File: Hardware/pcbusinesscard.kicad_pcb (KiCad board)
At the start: 2 copper layers, 89 x 51 mm, 0 parts

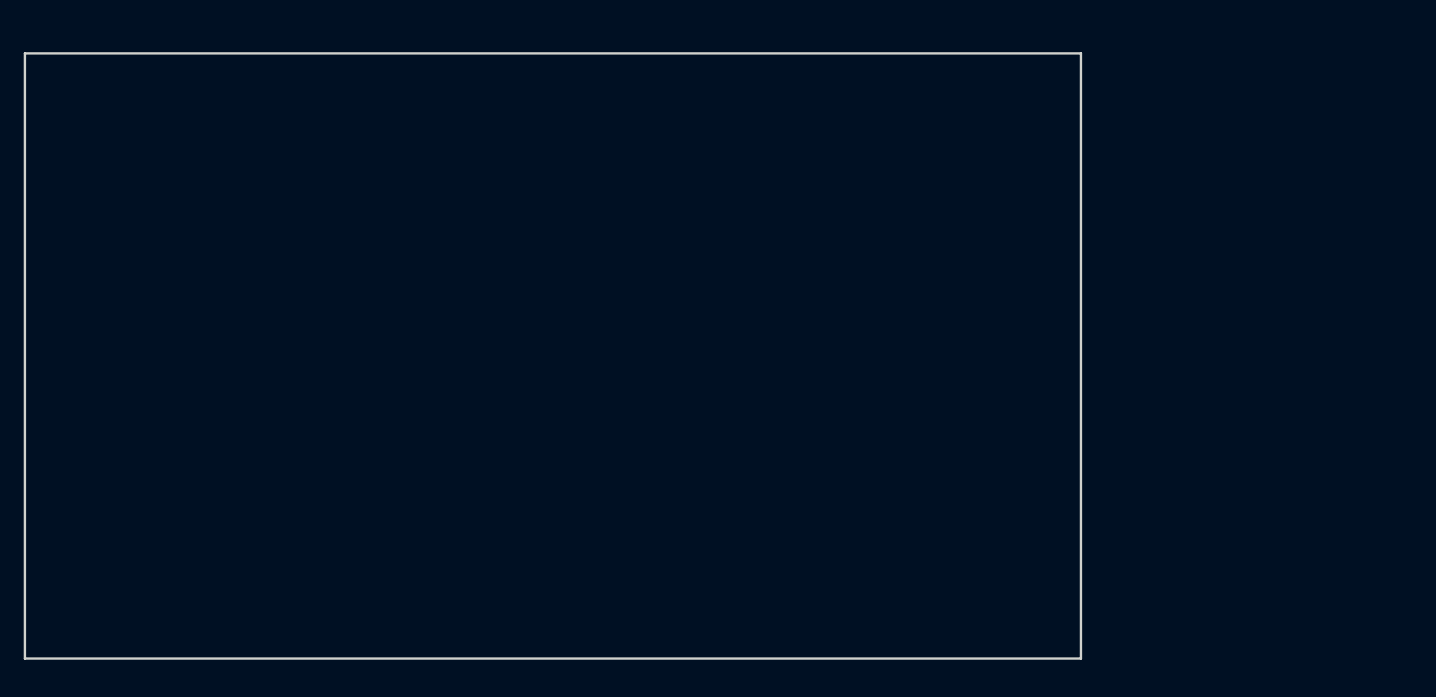
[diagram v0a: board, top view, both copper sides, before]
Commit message: Overhaul entire design with RP2040
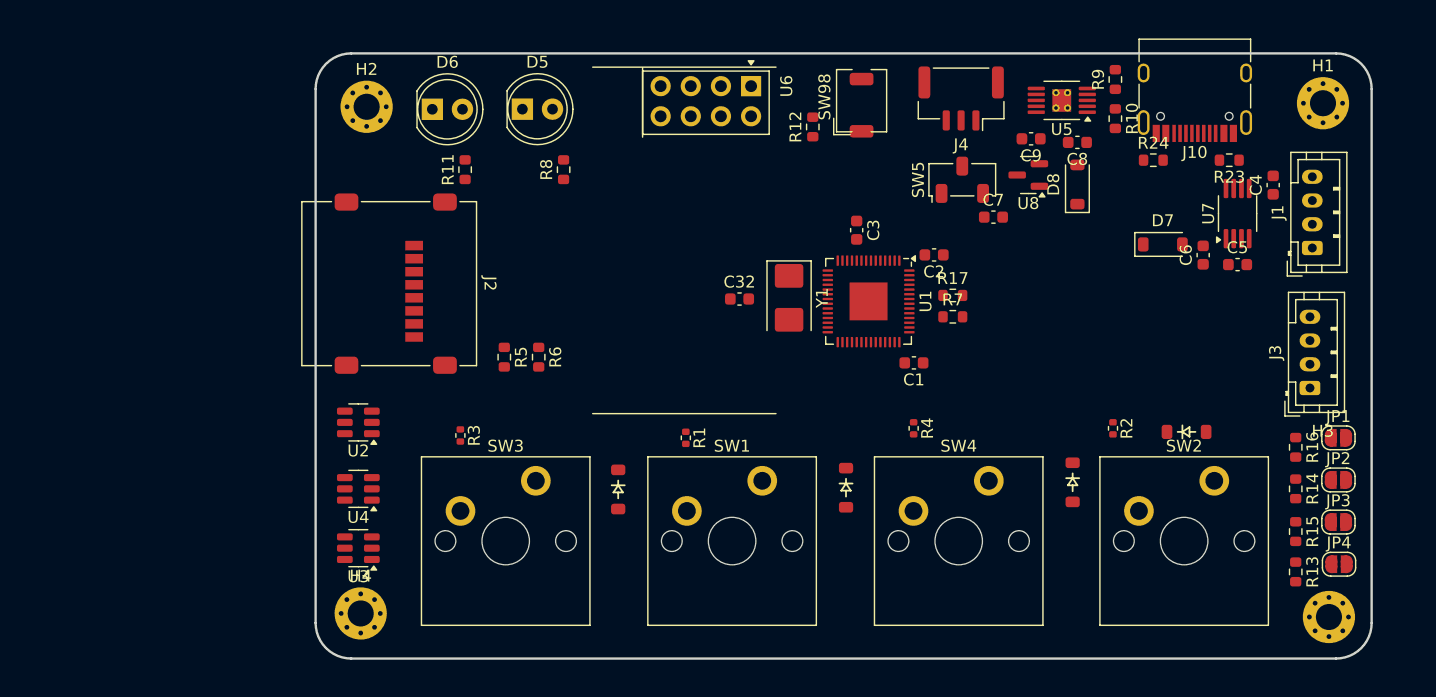
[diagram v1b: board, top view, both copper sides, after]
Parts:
- added C1: 1u, Capacitor_SMD:C_0603_1608Metric, F.Cu at (113.9, 63.1)
- added C2: 1u, Capacitor_SMD:C_0603_1608Metric, F.Cu at (115.6, 54.0)
- added C3: 1u, Capacitor_SMD:C_0603_1608Metric, F.Cu at (109.1, 51.9)
- added C32: 1u, Capacitor_SMD:C_0603_1608Metric, F.Cu at (99.2, 57.7)
- added C4: 1u, Capacitor_SMD:C_0603_1608Metric, F.Cu at (144.2, 48.1)
- added C5: 10n, Capacitor_SMD:C_0603_1608Metric, F.Cu at (141.2, 54.8)
- added C6: 10u, Capacitor_SMD:C_0603_1608Metric, F.Cu at (138.3, 54.0)
- added C7: 1u, Capacitor_SMD:C_0603_1608Metric, F.Cu at (120.6, 50.8)
- added C8: 1u, Capacitor_SMD:C_0603_1608Metric, F.Cu at (127.7, 44.5)
- added C9: 1u, Capacitor_SMD:C_0603_1608Metric, F.Cu at (123.8, 44.2)
- added D1: ESC, ScottoKeebs_Components:Diode_SOD-123, F.Cu at (108.2, 73.6)
- added D2: ~/`, ScottoKeebs_Components:Diode_SOD-123, F.Cu at (136.9, 68.9)
- added D3: 1, ScottoKeebs_Components:Diode_SOD-123, F.Cu at (89.0, 73.8)
- added D4: 2, ScottoKeebs_Components:Diode_SOD-123, F.Cu at (127.3, 73.2)
- added D5: LED_Small, LED_THT:LED_D5.0mm, F.Cu at (80.9, 41.7)
- added D6: LED_Small, LED_THT:LED_D5.0mm, F.Cu at (73.3, 41.7)
- added D7: MBR0520, Diode_SMD:D_SOD-123, F.Cu at (134.9, 53.1)
- added D8: MBR0520, Diode_SMD:D_SOD-123, F.Cu at (127.7, 48.0)
- added H1: MountingHole_Pad, MountingHole:MountingHole_2.2mm_M2_Pad_Via, F.Cu at (148.4, 41.2)
- added H2: MountingHole_Pad, MountingHole:MountingHole_2.2mm_M2_Pad_Via, F.Cu at (67.8, 41.5)
- added H3: MountingHole_Pad, MountingHole:MountingHole_2.2mm_M2_Pad_Via, F.Cu at (148.9, 84.5)
- added H4: MountingHole_Pad, MountingHole:MountingHole_2.2mm_M2_Pad_Via, F.Cu at (67.3, 84.2)
- added J1: Conn_01x04_Pin, Connector_JST:JST_PH_B4B-PH-K_1x04_P2.00mm_Vertical, F.Cu at (147.5, 53.4)
- added J10: USB_C_Receptacle_USB2.0, Connector_USB:USB_C_Receptacle_HRO_TYPE-C-31-M-12, F.Cu at (137.6, 39.7)
- added J2: Micro_SD_Card, Connector_Card:microSD_HC_Molex_47219-2001, F.Cu at (69.7, 56.4)
- added J3: Conn_01x04_Pin, Connector_JST:JST_PH_B4B-PH-K_1x04_P2.00mm_Vertical, F.Cu at (147.3, 65.2)
- added J4: Conn_01x03, Connector_JST:JST_GH_SM03B-GHS-TB_1x03-1MP_P1.25mm_Horizontal, F.Cu at (117.9, 40.8)
- added JP1: SolderJumper_2_Open, Jumper:SolderJumper-2_P1.3mm_Open_RoundedPad1.0x1.5mm, F.Cu at (149.7, 69.4)
- added JP2: SolderJumper_2_Open, Jumper:SolderJumper-2_P1.3mm_Open_RoundedPad1.0x1.5mm, F.Cu at (149.7, 73.0)
- added JP3: SolderJumper_2_Open, Jumper:SolderJumper-2_P1.3mm_Open_RoundedPad1.0x1.5mm, F.Cu at (149.7, 76.5)
- added JP4: SolderJumper_2_Open, Jumper:SolderJumper-2_P1.3mm_Open_RoundedPad1.0x1.5mm, F.Cu at (149.8, 80.1)
- added R1: 100, Resistor_SMD:R_0402_1005Metric, F.Cu at (94.7, 69.4)
- added R10: 1k, Resistor_SMD:R_0603_1608Metric, F.Cu at (130.9, 42.5)
- added R11: 1.5k, Resistor_SMD:R_0603_1608Metric, F.Cu at (76.1, 46.8)
- added R12: 10k, Resistor_SMD:R_0603_1608Metric, F.Cu at (105.4, 43.2)
- added R13: 10k, Resistor_SMD:R_0603_1608Metric, F.Cu at (146.1, 80.7)
- added R14: 10k, Resistor_SMD:R_0603_1608Metric, F.Cu at (146.1, 73.7)
- added R15: 10k, Resistor_SMD:R_0603_1608Metric, F.Cu at (146.1, 77.3)
- added R16: 10k, Resistor_SMD:R_0603_1608Metric, F.Cu at (146.1, 70.2)
- added R17: 22, Resistor_SMD:R_0603_1608Metric, F.Cu at (117.2, 57.4)
- added R2: 100, Resistor_SMD:R_0402_1005Metric, F.Cu at (130.7, 68.6)
- added R23: 5.1K, Resistor_SMD:R_0603_1608Metric, F.Cu at (140.5, 46.0)
- added R24: 5.1K, Resistor_SMD:R_0603_1608Metric, F.Cu at (134.1, 46.0)
- added R3: 100, Resistor_SMD:R_0402_1005Metric, F.Cu at (75.7, 69.2)
- added R4: 100, Resistor_SMD:R_0402_1005Metric, F.Cu at (113.9, 68.6)
- added R5: 4.7k, Resistor_SMD:R_0603_1608Metric, F.Cu at (79.4, 62.6)
- added R6: 4.7k, Resistor_SMD:R_0603_1608Metric, F.Cu at (82.3, 62.6)
- added R7: 22, Resistor_SMD:R_0603_1608Metric, F.Cu at (117.2, 59.2)
- added R8: 1.5k, Resistor_SMD:R_0603_1608Metric, F.Cu at (84.4, 46.8)
- added R9: 2k, Resistor_SMD:R_0603_1608Metric, F.Cu at (130.9, 39.2)
- added SW1: ESC, ScottoKeebs_MX:MX_PCB_1.00u, F.Cu at (98.6, 78.1)
- added SW2: `, ScottoKeebs_MX:MX_PCB_1.00u, F.Cu at (136.7, 78.1)
- added SW3: 1, ScottoKeebs_MX:MX_PCB_1.00u, F.Cu at (79.5, 78.1)
- added SW4: 2, ScottoKeebs_MX:MX_PCB_1.00u, F.Cu at (117.7, 78.1)
- added SW5: SW_Nidec_CAS-120A1, Button_Switch_SMD:Nidec_Copal_CAS-120A, F.Cu at (118.0, 47.6)
- added SW98: SW_Push, ScottoKeebs_Miscellaneous:SW_DIP_SPSTx01_Slide_6.7x4.1mm_W6.73mm_P2.54mm_LowProfile_JPin, F.Cu at (109.5, 43.6)
- added U1: RP2040, Package_DFN_QFN:QFN-56-1EP_7x7mm_P0.4mm_EP3.2x3.2mm, F.Cu at (110.1, 57.9)
- added U2: 24AA025E-OT, Package_TO_SOT_SMD:SOT-23-6, F.Cu at (67.1, 68.1)
- added U3: 24AA025E-OT, Package_TO_SOT_SMD:SOT-23-6, F.Cu at (67.1, 78.7)
- added U4: 24AA025E-OT, Package_TO_SOT_SMD:SOT-23-6, F.Cu at (67.1, 73.7)
- added U5: BQ24090DGQ, Package_SO:HVSSOP-10-1EP_3x3mm_P0.5mm_EP1.57x1.88mm_ThermalVias, F.Cu at (126.4, 41.0)
- added U6: NRF24L01_Breakout, RF_Module:nRF24L01_Breakout, F.Cu at (100.2, 39.8)
- added U7: LT1762-3.3, Package_SO:MSOP-8_3x3mm_P0.65mm, F.Cu at (141.2, 50.5)
- added U8: MCP1700x-330xxTT, Package_TO_SOT_SMD:SOT-23, F.Cu at (123.6, 47.2)
- added Y1: 12MHz, Crystal:Crystal_SMD_5032-2Pin_5.0x3.2mm, F.Cu at (103.4, 57.6)
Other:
- outline, holes or cut-outs redrawn

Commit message: adding to layout
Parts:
- added C10: 1u, Capacitor_SMD:C_0603_1608Metric, F.Cu at (108.4, 64.9)
- added D10: LED_Small, LED_SMD:LED_0805_2012Metric, F.Cu at (136.0, 61.5)
- added D9: LED_Small, LED_SMD:LED_0805_2012Metric, F.Cu at (132.7, 61.5)
- added R18: 1.5k, Resistor_SMD:R_0603_1608Metric, F.Cu at (133.0, 58.0)
- added R19: 1.5k, Resistor_SMD:R_0603_1608Metric, F.Cu at (135.5, 58.0)
- C1: value 1u -> 4.7u
- moved D3 7.19 mm to (89.8, 66.6), turned to 180 degrees
- moved C32 5.52 mm to (102.8, 61.9)
- moved R5 5.30 mm to (84.7, 62.6)
- moved R15 4.40 mm to (146.1, 72.9), turned to 180 degrees
- moved C1 3.42 mm to (117.1, 61.8)
- moved R6 2.91 mm to (79.4, 62.8)
- moved R14 2.70 mm to (146.1, 76.4), turned to 180 degrees
- moved D5 2.55 mm to (83.5, 41.8), turned to 180 degrees
- moved D4 1.85 mm to (127.4, 71.3)
- moved Y1 1.40 mm to (102.0, 57.6)
- moved R13 1.20 mm to (146.0, 79.5), turned to 180 degrees
- moved R16 0.90 mm to (146.1, 69.3), turned to 180 degrees
- moved R17 0.80 mm to (117.2, 58.2)
- moved R7 0.80 mm to (117.2, 60.0)
- moved H3 0.64 mm to (148.5, 84.0)
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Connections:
- net Net-(J10-D+-PadA6) renamed /d+
- net Net-(J10-D--PadA7) renamed /d-
- H1 pad 1: VDD -> VBUS
- H2 pad 1: VBUS -> VBAT
- H3 pad 1: VBAT -> +3.3V
- J1 pad 1: unconnected-(J1-Pin_1-Pad1) -> +3.3V
- J3 pad 1: unconnected-(J3-Pin_1-Pad1) -> +3.3V
- JP1 pad 2: VDD -> +3.3V
- JP2 pad 2: VDD -> +3.3V
- JP3 pad 2: VDD -> +3.3V
- JP4 pad 2: VDD -> +3.3V
- R1 pad 1: VDD -> +3.3V
- R11 pad 1: unconnected-(R11-Pad1) -> VBUS
- R12 pad 1: VDD -> +3.3V
- R2 pad 1: VDD -> +3.3V
- R3 pad 1: VDD -> +3.3V
- R4 pad 1: VDD -> +3.3V
- U1 pad 12: unconnected-(U1-GPIO9-Pad12) -> /SPI1_CS
- U1 pad 13: unconnected-(U1-GPIO10-Pad13) -> /SPI1_SCK
- U1 pad 15: unconnected-(U1-GPIO12-Pad15) -> /SPI1_MISO
- U1 pad 29: unconnected-(U1-GPIO18-Pad29) -> /RP_SCK0
- U1 pad 30: unconnected-(U1-GPIO19-Pad30) -> /RP_SDA0
- U1 pad 31: unconnected-(U1-GPIO20-Pad31) -> /SW_3
- U1 pad 34: unconnected-(U1-GPIO22-Pad34) -> /SW_1
- U1 pad 35: unconnected-(U1-GPIO23-Pad35) -> /SW_4
- U1 pad 36: unconnected-(U1-GPIO24-Pad36) -> /SW_2
- U1 pad 37: unconnected-(U1-GPIO25-Pad37) -> /ADD_B3
- U1 pad 38: unconnected-(U1-GPIO26_ADC0-Pad38) -> /ADD_B2
- U1 pad 39: unconnected-(U1-GPIO27_ADC1-Pad39) -> /ADD_B1
- U1 pad 40: unconnected-(U1-GPIO28_ADC2-Pad40) -> /ADD_B0
- U1 pad 52: /SPI1_SCK -> unconnected-(U1-QSPI_SCLK-Pad52)
- U1 pad 55: /SPI1_MISO -> unconnected-(U1-QSPI_SD1-Pad55)
- U1 pad 9: unconnected-(U1-GPIO7-Pad9) -> /SPI1_MOSI
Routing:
- net +3.3V: track 0.00 -> 99.4 mm, vias 0 -> 15
- net /RP_SCK0: track 0.00 -> 73.8 mm
- net VBUS: track 0.00 -> 73.7 mm, vias 0 -> 2
- net GND: track 0.00 -> 61.1 mm, vias 0 -> 16
- net /RP_SDA0: track 0.00 -> 59.3 mm
- net /ADD_B3: track 0.00 -> 52.2 mm
- net /RP_SWCK: track 0.00 -> 49.5 mm, vias 0 -> 1
- net /ADD_B2: track 0.00 -> 48.7 mm
- net /RP_SWDIO: track 0.00 -> 48.5 mm, vias 0 -> 1
- net /ADD_B1: track 0.00 -> 45.0 mm
- net Net-(D5-K): track 0.00 -> 44.6 mm
- net /SPI1_MOSI: track 0.00 -> 42.2 mm
- net /ADD_B0: track 0.00 -> 41.6 mm
- net /SPI1_CS: track 0.00 -> 38.7 mm, vias 0 -> 2
- net /SPI1_SCK: track 0.00 -> 38.7 mm
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- added copper zone on In2.Cu, net +3.3V
- added copper zone on B.Cu, net GND
- added copper zone on F.Cu, net GND
- added copper zone on In1.Cu, net GND
- added copper zone on F.Cu, net VBAT
- added copper zone on In2.Cu, net VBAT
- added copper zone on F.Cu, net VBUS
- added copper zone on In2.Cu, net VBUS
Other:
- copper layers 2 -> 4

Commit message: Finish Draft
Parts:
- removed D7, D8: MBR0520, Diode_SMD:D_SOD-123
- added C11: 1u, Capacitor_SMD:C_0603_1608Metric, F.Cu at (122.0, 56.6)
- added J5: Conn_ST_STDC14, Connector_PinHeader_1.27mm:PinHeader_2x07_P1.27mm_Vertical, F.Cu at (136.0, 60.8)
- added R20: 1.5k, Resistor_SMD:R_0603_1608Metric, F.Cu at (127.7, 51.6)
- added R21: 10k, Resistor_SMD:R_0603_1608Metric, F.Cu at (120.9, 61.9)
- added R22: 10k, Resistor_SMD:R_0603_1608Metric, F.Cu at (114.7, 44.2)
- added TP1: TestPoint, TestPoint:TestPoint_Keystone_5010-5014_Multipurpose, F.Cu at (84.8, 57.3)
- added TP2: TestPoint, TestPoint:TestPoint_Keystone_5010-5014_Multipurpose, F.Cu at (80.2, 57.2)
- added TP3: TestPoint, TestPoint:TestPoint_Keystone_5010-5014_Multipurpose, F.Cu at (93.3, 57.3)
- added TP4: TestPoint, TestPoint:TestPoint_Keystone_5010-5014_Multipurpose, F.Cu at (89.1, 57.3)
- added TP5: TestPoint, TestPoint:TestPoint_Keystone_5010-5014_Multipurpose, F.Cu at (97.6, 57.3)
- added U9: TPS2116DRL, Package_TO_SOT_SMD:SOT-583-8, F.Cu at (128.5, 49.1)
- J3: footprint Connector_JST:JST_PH_B4B-PH-K_1x04_P2.00mm_Vertical -> Connector_PinHeader_2.54mm:PinHeader_1x04_P2.54mm_Vertical
- J4: footprint Connector_JST:JST_GH_SM03B-GHS-TB_1x03-1MP_P1.25mm_Horizontal -> Connector_JST:JST_ZH_B3B-ZR_1x03_P1.50mm_Vertical
- moved R19 7.63 mm to (127.9, 58.6), turned to 0 degrees
- moved J1 6.24 mm to (149.2, 47.4), turned to -90 degrees
- moved R18 6.06 mm to (127.8, 61.1), turned to 0 degrees
- moved D10 5.43 mm to (131.5, 58.5), turned to 180 degrees
- moved J4 2.45 mm to (115.5, 40.3), turned to 0 degrees
- moved J3 2.14 mm to (149.4, 65.6), turned to 180 degrees
- moved C3 1.40 mm to (109.1, 50.5)
- moved D9 1.25 mm to (131.5, 61.2), turned to 180 degrees
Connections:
- net Net-(D7-A) renamed VBUS_LDO
- net Net-(D8-A) renamed VBAT_LDO
- C4 pad 1: Net-(U7-GND) -> GND
- C6 pad 1: Net-(U7-GND) -> GND
- J1 pad 2: /nRF_UART_RX -> /nRF_UART_TX
- J1 pad 3: /nRF_UART_TX -> /nRF_UART_RX
- R18 pad 1: unconnected-(R18-Pad1) -> /status_LED0
- R19 pad 1: unconnected-(R19-Pad1) -> /status_LED1
- SW5 pad 1: unconnected-(SW5-C-Pad1) -> VBAT
- U1 pad 2: unconnected-(U1-GPIO0-Pad2) -> /nRF_CE
- U1 pad 27: unconnected-(U1-GPIO16-Pad27) -> /nRF_UART_TX
- U1 pad 28: unconnected-(U1-GPIO17-Pad28) -> /nRF_UART_RX
- U1 pad 3: unconnected-(U1-GPIO1-Pad3) -> /SPI0_CSN
- U1 pad 4: unconnected-(U1-GPIO2-Pad4) -> /SPI0_SCK
- U1 pad 41: unconnected-(U1-GPIO29_ADC3-Pad41) -> Net-(U1-GPIO29_ADC3)
- U1 pad 5: unconnected-(U1-GPIO3-Pad5) -> /SPI0_MOSI
- U1 pad 51: unconnected-(U1-QSPI_SD3-Pad51) -> /status_LED0
- U1 pad 52: unconnected-(U1-QSPI_SCLK-Pad52) -> /status_LED1
- U1 pad 6: unconnected-(U1-GPIO4-Pad6) -> /SPI0_MISO
- U1 pad 7: unconnected-(U1-GPIO5-Pad7) -> /nRF_IRQ
- U6 pad 3: unconnected-(U6-CE-Pad3) -> /nRF_CE
- U6 pad 4: unconnected-(U6-~{CSN}-Pad4) -> /SPI0_CSN
- U6 pad 5: unconnected-(U6-SCK-Pad5) -> /SPI0_SCK
- U6 pad 6: unconnected-(U6-MOSI-Pad6) -> /SPI0_MOSI
- U6 pad 7: unconnected-(U6-MISO-Pad7) -> /SPI0_MISO
- U6 pad 8: unconnected-(U6-IRQ-Pad8) -> /nRF_IRQ
- U7 pad 4: Net-(U7-GND) -> GND
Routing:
- net GND: track 61.1 -> 144.6 mm, vias 16 -> 60
- net /nRF_UART_TX: track 0.00 -> 52.4 mm, vias 0 -> 1
- net /nRF_UART_RX: track 0.00 -> 52.3 mm, vias 0 -> 1
- net /~{RESET}: track 22.6 -> 62.5 mm, vias 2 -> 5
- net +3.3V: track 99.4 -> 137.1 mm, vias 15 -> 18
- net Net-(U1-GPIO29_ADC3): track 0.00 -> 29.6 mm, vias 0 -> 2
- net /SPI1_MOSI: track 42.2 -> 71.4 mm, vias 0 -> 1
- net /SPI0_MISO: track 0.00 -> 28.3 mm
- net unconnected-(U1-GPIO29_ADC3-Pad41): track 27.3 -> 0.00 mm, vias 2 -> 0
- net /SPI0_SCK: track 0.00 -> 26.7 mm
- net /nRF_IRQ: track 0.00 -> 25.7 mm
- net /nRF_CE: track 0.00 -> 25.2 mm
- net /SPI0_MOSI: track 0.00 -> 24.2 mm
- net /SPI0_CSN: track 0.00 -> 23.9 mm, vias 0 -> 3
- net /SPI1_SCK: track 38.7 -> 62.4 mm, vias 0 -> 1
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
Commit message: Finish first draft of routing
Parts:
- removed D2: ~/`, ScottoKeebs_Components:Diode_SOD-123
- removed D3: 1, ScottoKeebs_Components:Diode_SOD-123
- removed D4: 2, ScottoKeebs_Components:Diode_SOD-123
- removed J1: Conn_01x04_Pin, Connector_JST:JST_PH_B4B-PH-K_1x04_P2.00mm_Vertical
- removed J3: Conn_01x04_Pin, Connector_PinHeader_2.54mm:PinHeader_1x04_P2.54mm_Vertical
- removed R2: 100, Resistor_SMD:R_0402_1005Metric
- removed SW2: `, ScottoKeebs_MX:MX_PCB_1.00u
- removed U6: NRF24L01_Breakout, RF_Module:nRF24L01_Breakout
- removed U7: LT1762-3.3, Package_SO:MSOP-8_3x3mm_P0.65mm
- added C12: 22p, Capacitor_SMD:C_0402_1005Metric, F.Cu at (93.9, 46.9)
- added C13: 22p, Capacitor_SMD:C_0402_1005Metric, F.Cu at (109.6, 47.9)
- added C14: 33nF, Capacitor_SMD:C_0402_1005Metric, F.Cu at (84.7, 54.9)
- added C15: 1n, Capacitor_SMD:C_0402_1005Metric, F.Cu at (82.5, 51.5)
- added C16: 10n, Capacitor_SMD:C_0402_1005Metric, F.Cu at (90.5, 51.0)
- added C17: 1p, Capacitor_SMD:C_0402_1005Metric, F.Cu at (85.9, 47.2)
- added C18: 1p, Capacitor_SMD:C_0402_1005Metric, F.Cu at (87.3, 47.9)
- added D11: LED_Small, LED_SMD:LED_0805_2012Metric, F.Cu at (139.5, 53.3)
- added D12: LED_Small, LED_SMD:LED_0805_2012Metric, F.Cu at (140.6, 56.7)
- added D8: LED_Small, LED_SMD:LED_0805_2012Metric, F.Cu at (135.9, 53.3)
- added IFA1: ~, RF_Antenna:Texas_SWRA117D_2.4GHz_Right, F.Cu at (91.2, 44.4)
- added J6: Conn_01x04_Pin, Connector_JST:JST_PH_B4B-PH-K_1x04_P2.00mm_Vertical, F.Cu at (130.7, 84.1)
- added J7: Conn_01x04_Pin, Connector_JST:JST_PH_B4B-PH-K_1x04_P2.00mm_Vertical, F.Cu at (66.5, 76.7)
- added L1: 3.9n, Inductor_SMD:L_0402_1005Metric, F.Cu at (84.4, 48.7)
- added L2: 33u, Inductor_SMD:L_0402_1005Metric, F.Cu at (133.8, 63.5)
- added L3: 8.2n, Inductor_SMD:L_0402_1005Metric, F.Cu at (83.6, 47.6)
- added L4: 2.7n, Inductor_SMD:L_0402_1005Metric, F.Cu at (82.2, 49.1)
- added Q1: MMBT3904, Package_TO_SOT_SMD:SOT-23, F.Cu at (140.3, 61.9)
- added Q2: MMBT3904, Package_TO_SOT_SMD:SOT-23, F.Cu at (143.8, 52.3)
- added Q3: MMBT3904, Package_TO_SOT_SMD:SOT-23, F.Cu at (137.9, 50.1)
- added Q4: MMBT3904, Package_TO_SOT_SMD:SOT-23, F.Cu at (134.4, 60.5)
- added Q5: MMBT3904, Package_TO_SOT_SMD:SOT-23, F.Cu at (132.5, 54.1)
- added R25: 22k, Resistor_SMD:R_0603_1608Metric, F.Cu at (82.2, 54.0)
- added R26: 1300, Resistor_SMD:R_0402_1005Metric, F.Cu at (129.2, 58.5)
- added R27: 1.3k, Resistor_SMD:R_0402_1005Metric, F.Cu at (129.2, 57.2)
- added R28: 1.3k, Resistor_SMD:R_0402_1005Metric, F.Cu at (129.1, 59.9)
- added R29: 1.3k, Resistor_SMD:R_0402_1005Metric, F.Cu at (129.2, 56.0)
- added R30: 400, Resistor_SMD:R_0402_1005Metric, F.Cu at (141.9, 59.4)
- added R31: 400, Resistor_SMD:R_0402_1005Metric, F.Cu at (134.1, 50.8)
- added R32: 400, Resistor_SMD:R_0402_1005Metric, F.Cu at (137.7, 61.8)
- added R33: 400, Resistor_SMD:R_0402_1005Metric, F.Cu at (131.7, 57.8)
- added U10: NRF24L01, Package_DFN_QFN:QFN-20-1EP_4x4mm_P0.5mm_EP2.5x2.5mm, F.Cu at (86.6, 52.1)
- added U12: LM2596S-3.3, Package_TO_SOT_SMD:TO-263-5_TabPin3, F.Cu at (133.7, 74.8)
- added Y2: Crystal, Crystal:Crystal_SMD_HC49-SD, F.Cu at (101.4, 47.9)
- C5: value 10n -> 4.7pF; footprint Capacitor_SMD:C_0603_1608Metric -> Capacitor_SMD:C_0402_1005Metric
- D1: value ESC -> SS34; footprint ScottoKeebs_Components:Diode_SOD-123 -> Diode_SMD:D_SMA
- J5: footprint Connector_PinHeader_1.27mm:PinHeader_2x07_P1.27mm_Vertical -> Connector:Tag-Connect_TC2070-IDC-FP_2x07_P1.27mm_Vertical
- R18: value 1.5k -> 400; footprint Resistor_SMD:R_0603_1608Metric -> Resistor_SMD:R_0402_1005Metric
- R19: value 1.5k -> 1300; footprint Resistor_SMD:R_0603_1608Metric -> Resistor_SMD:R_0402_1005Metric
- moved C5 53.4 mm to (88.6, 45.6)
- moved D1 46.7 mm to (148.9, 50.6)
- moved U3 29.0 mm to (93.2, 66.1), turned to 90 degrees
- moved U4 22.5 mm to (88.2, 66.0), turned to 90 degrees
- moved C4 19.3 mm to (140.5, 67.0)
- moved R18 17.3 mm to (141.5, 50.6), turned to -126 degrees
- moved U2 14.3 mm to (81.3, 66.2), turned to 90 degrees
- moved C6 11.9 mm to (131.1, 63.5), turned to 0 degrees
- moved J5 11.6 mm to (147.6, 61.5), turned to -90 degrees
- moved R4 9.48 mm to (107.4, 75.5)
- moved R1 8.13 mm to (89.1, 75.3)
- moved D9 6.63 mm to (137.7, 58.8), turned to -90 degrees
- moved D10 3.76 mm to (134.8, 56.7), turned to -162 degrees
- moved R8 3.61 mm to (80.8, 46.6)
- moved TP2 3.26 mm to (81.2, 60.3)
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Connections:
- net /RP_SCK0 renamed /RP_I2C0_SDA
- net /RP_SDA0 renamed /RP_I2C0_SCK
- net VBAT_LDO renamed VBAT_REG
- C5 pad 1: Net-(U7-SENSE) -> GND
- C6 pad 2: VBUS_LDO -> VBUS_REG
- D1 pad 1: /SW_1 -> VBUS_REG
- D1 pad 2: Net-(D1-A) -> GND
- D10 pad 1: GND -> Net-(D10-K)
- D9 pad 1: GND -> Net-(D9-K)
- J5 pad 13: unconnected-(J5-VCP_RX-Pad13) -> /RP_UART_RX
- J5 pad 14: unconnected-(J5-VCP_TX-Pad14) -> /RP_UART_TX
- R18 pad 1: /status_LED0 -> +3.3V
- R18 pad 2: Net-(D9-A) -> Net-(D11-A)
- R19 pad 1: /status_LED1 -> /LED_1
- R19 pad 2: Net-(D10-A) -> Net-(Q1-B)
- SW1 pad 2: Net-(D1-A) -> /SW_1
- SW3 pad 2: Net-(D3-A) -> /SW_3
- SW4 pad 2: Net-(D4-A) -> /SW_4
- U1 pad 2: /nRF_CE -> /SPI0_MISO
- U1 pad 27: /nRF_UART_TX -> /RP_UART_TX
- U1 pad 28: /nRF_UART_RX -> /RP_UART_RX
- U1 pad 32: unconnected-(U1-GPIO21-Pad32) -> /SW_1
- U1 pad 34: /SW_1 -> /SW_4
- U1 pad 35: /SW_4 -> /RP_I2C1_SDA
- U1 pad 36: /SW_2 -> /RP_I2C1_SCL
- U1 pad 4: /SPI0_SCK -> /nRF_IRQ
- U1 pad 51: /status_LED0 -> /LED_1
- U1 pad 52: /status_LED1 -> /LED_0
- U1 pad 53: unconnected-(U1-QSPI_SD0-Pad53) -> /LED_4
- U1 pad 54: unconnected-(U1-QSPI_SD2-Pad54) -> /LED_2
- U1 pad 55: unconnected-(U1-QSPI_SD1-Pad55) -> /LED_3
- U1 pad 6: /SPI0_MISO -> unconnected-(U1-GPIO4-Pad6)
- U1 pad 7: /nRF_IRQ -> /nRF_CE
- U1 pad 8: unconnected-(U1-GPIO6-Pad8) -> /SPI0_SCK
- U9 pad 3: VBUS_LDO -> VBUS_REG
- U9 pad 4: VBUS_LDO -> VBUS_REG
- U9 pad 5: VBUS_LDO -> VBUS_REG
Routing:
- net /RP_I2C1_SCL: track 0.00 -> 113.0 mm
- net /RP_I2C1_SDA: track 0.00 -> 109.3 mm
- net VBUS_REG: track 0.00 -> 58.3 mm, vias 0 -> 3
- net /nRF_UART_TX: track 52.4 -> 0.00 mm, vias 1 -> 0
- net /nRF_UART_RX: track 52.3 -> 0.00 mm, vias 1 -> 0
- net /RP_UART_RX: track 0.00 -> 49.3 mm, vias 0 -> 2
- net /RP_UART_TX: track 0.00 -> 47.3 mm, vias 0 -> 2
- net GND: track 144.6 -> 181.1 mm, vias 60 -> 98
- net /SW_2: track 30.7 -> 0.00 mm
- net /RP_I2C0_SDA: track 79.2 -> 52.3 mm
- net +3.3V: track 137.1 -> 113.3 mm, vias 18 -> 25
- net Net-(U10-XC1): track 0.00 -> 22.6 mm
- net Net-(U10-XC2): track 0.00 -> 22.5 mm
- net VBUS_LDO: track 19.9 -> 0.00 mm, vias 2 -> 0
- net Net-(Q2-B): track 0.00 -> 17.9 mm
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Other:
- board text added: "ADD0"
- board text added: "ADD1"
- board text added: "ADD2"
- board text added: "ADD3"
- board text added: "GND"
- board text added: "VBAT"
- board text added: "VBUS"
- board text added: "VDD"
